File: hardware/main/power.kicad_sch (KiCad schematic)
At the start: 59 parts, among them J1 USB-307HB-B-SU, J12 Interrupteur, J2 Batterie 18650, Q1 AO3401A, Q2 2N7002, U10 FS8205, U12 USBLC6-2SC6, U5 AP2112M-3.3, U6 AP2112K-3.3, U7 MT3608, U8 BQ24075RGTR, U9 DW01A

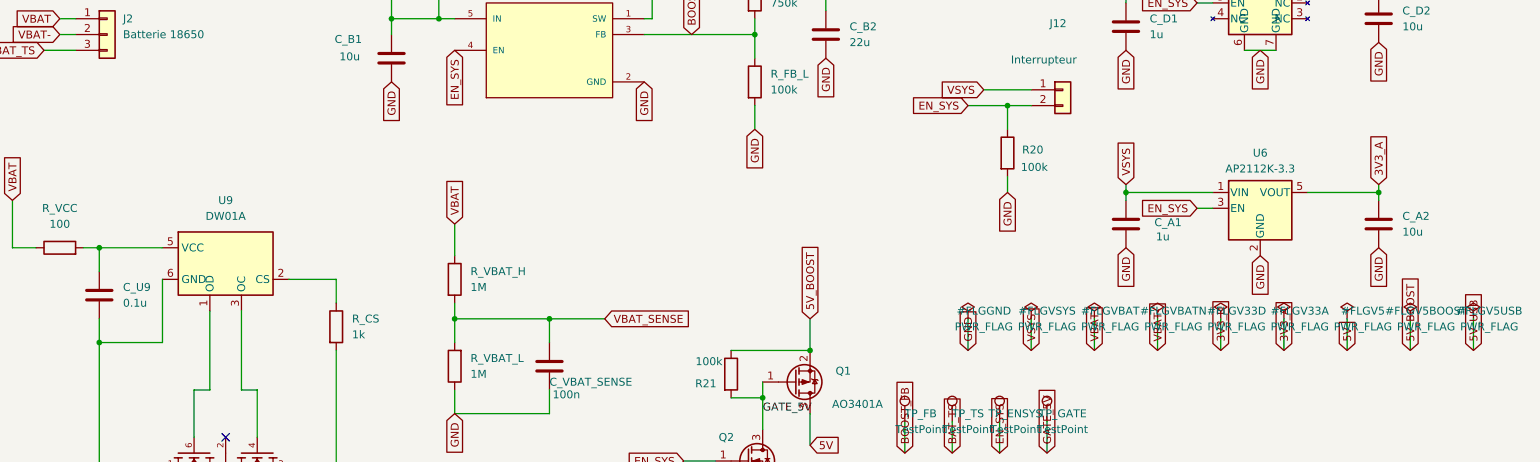
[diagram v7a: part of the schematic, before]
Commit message: hardware+tools: 5 dernieres erreurs ERC + deux bugs de mes outils
ERC 48 -> 5 -> 0 attendu. Les 5 restantes venaient toutes de mes PWR_FLAG :
j'en avais pose neuf, soit trois de trop, et mal nommes.

- 3V3_D et 3V3_A sont deja pilotes par une vraie pin « power output » (les VOUT
  des deux LDO) : deux sources sur un meme net = erreur. Flags retires.
- VSYS : la sortie du bq24075 est une sortie d'alimentation. Plutot que d'y
  ajouter un flag, OUT_10 est typee power_out — c'est elle qui pilote le net.
  OUT_11 reste passive (les deux broches sont la meme sortie sur le QFN).
- U9.VCC (DW01A) n'arrive qu'a travers R_VCC, aucune pin ne le pilote : net
  nomme DW_VCC et flag ajoute. C'etait le seul flag reellement manquant.
- annotation : KiCad attend « prefixe + numero ». #FLGGND -> #FLG01..#FLG07.

DEUX BUGS DE MES OUTILS, corriges :
1. kicad_edit.symbol_block() delimitait un symbole jusqu'au symbole SUIVANT.
   Or des fils et labels sont intercales entre symboles : une suppression les
   emportait silencieusement. Remplace par un comptage de parentheses.
   C'est ce bug qui faisait echouer le script, et il aurait pu casser le schema
   sans bruit.
2. drop_wire() comparait les coordonnees comme des chaines, alors que KiCad
   ecrit « 165.10000000000002 ». Comparaison numerique + drop_label() ajoute.

kicad_netlist.py --check : nouvelle verification des fils mal raccordes, dont
le cas precis qui m'avait echappe sur la jonction L1 — une extremite posee au
milieu d'un autre fil sans jonction, que KiCad ne connecte pas alors que la
connectivite logique le suggere. Le schema passe ce controle sans rien signaler.
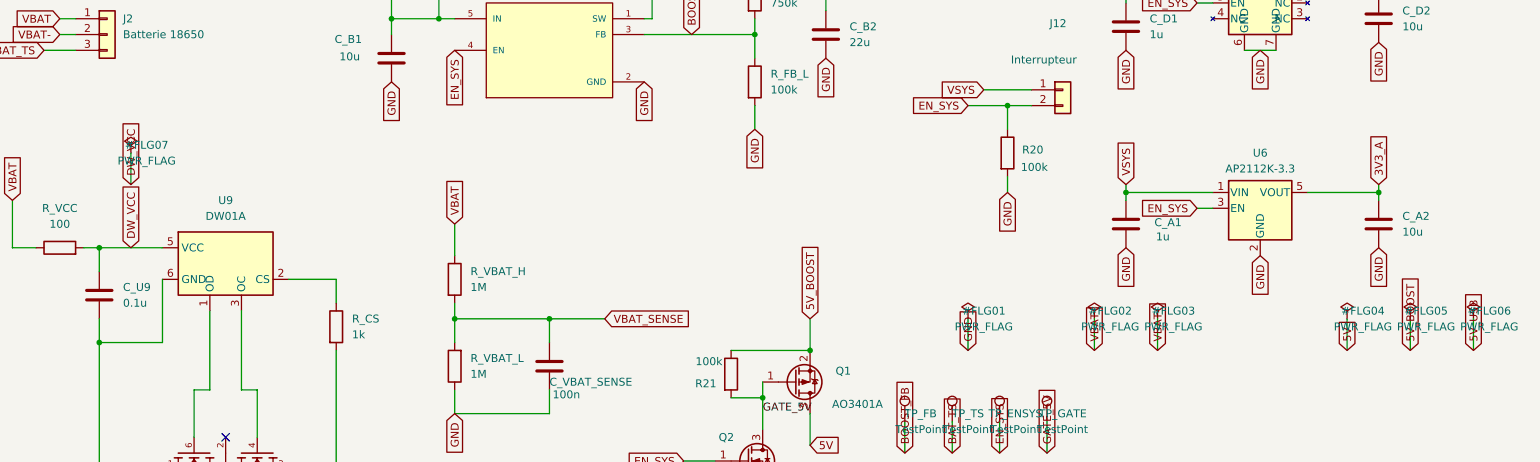
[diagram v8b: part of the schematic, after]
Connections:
- net DW_VCC: now reaches C_U9.1, R_VCC.2, U9.5 (VCC)
